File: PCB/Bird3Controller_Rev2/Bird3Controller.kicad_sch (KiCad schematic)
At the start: 49 parts, among them IC2 LM3519MK-20_NOPB, IC3 LM3405AXMY_NOPB, J1 Bird 3 24-pin Connector, J2 TXW154028S0 Connector, J3 2171800001, SW1 SW_Boot, SW2 SW_Reset, U1 ESP32-S3-WROOM-1, U3 SN65HVD231, U4 LMR36520ADDAR

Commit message: Add 22-pin connector, new headlight circuit, etc. for Rev 2
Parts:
- removed C23: 10u, Capacitor_SMD:C_0805_2012Metric_Pad1.18x1.45mm_HandSolder, symbol Device:C_Small
- removed C24: 0.01u, Capacitor_SMD:C_0805_2012Metric_Pad1.18x1.45mm_HandSolder, symbol Device:C_Small
- removed C25, C26: 1u, Capacitor_SMD:C_0805_2012Metric_Pad1.18x1.45mm_HandSolder, symbol Device:C_Small
- removed C4: 4n7, Capacitor_SMD:C_0805_2012Metric_Pad1.18x1.45mm_HandSolder, symbol Device:C_Small
- removed D2: D_Small, Diode_SMD:D_0805_2012Metric_Pad1.15x1.40mm_HandSolder, symbol Device:D_Small
- removed D4: D_Schottky_Small, Diode_SMD:D_0805_2012Metric_Pad1.15x1.40mm_HandSolder, symbol Device:D_Schottky_Small
- removed D7: PRTR5V0U2X, Package_TO_SOT_SMD:SOT-143, symbol Power_Protection:PRTR5V0U2X
- removed IC3: LM3405AXMY_NOPB, Bird3Controller:SOP65P490X109-9N, symbol Bird3Controller:LM3405AXMY_NOPB
- removed J3: 2171800001, Bird3Controller:MOLEX_2171800001, symbol Bird3Controller:2171800001
- removed L5: 27u, Bird3Controller:SRR1240270M, symbol Device:L_Small
- removed R14: 0.953Ω, Resistor_SMD:R_0805_2012Metric_Pad1.20x1.40mm_HandSolder, symbol Device:R_Small_US
- removed R4: 1M, Resistor_SMD:R_0805_2012Metric_Pad1.20x1.40mm_HandSolder, symbol Device:R_Small_US
- added C8: 10u, Capacitor_SMD:C_0805_2012Metric_Pad1.18x1.45mm_HandSolder, symbol Device:C_Small
- added J3: 87832-2220, Bird3Controller:878322220, symbol Bird3Controller:Bird 3 22-Pin Connector
- added J4: ~, Bird3Controller:Adafruit USB-C Breakout, symbol Bird3Controller:Adafruit_4090_USBC_BOB
- added L1: 100u, Bird3Controller:SRR1240270M, symbol Device:L_Small
- added R7: 0.200Ω, Resistor_SMD:R_0805_2012Metric_Pad1.20x1.40mm_HandSolder, symbol Device:R_Small_US
- added TP1: LCD_BL+, Bird3Controller:TestPointBridge_2Pads_D1.5mm, symbol Bird3Controller:TestPoint_Junction
- added TP2: 3V3, Bird3Controller:TestPointBridge_2Pads_D1.5mm, symbol Bird3Controller:TestPoint_Junction
- added TP3: VIN, Bird3Controller:TestPointBridge_2Pads_D1.5mm, symbol Bird3Controller:TestPoint_Junction
- added TP4: LED+, Bird3Controller:TestPointBridge_2Pads_D1.5mm, symbol Bird3Controller:TestPoint_Junction
- added TP5: LED-, Bird3Controller:TestPointBridge_2Pads_D1.5mm, symbol Bird3Controller:TestPoint_Junction
- added TP_Boot1: TestPoint_2Pole, Bird3Controller:TestPoint_2Pads_D1.0mm, symbol Connector:TestPoint_2Pole
- added U2: ~, Bird3Controller:Diodes_SO-8EP, symbol Bird3Controller:AL8862
- D3: Digikey Part Number (none) -> 478-7800-1-ND; JLCPCB Part (none) -> C143773; Manufacturer_Name (none) -> KYOCERA AVX; Manufacturer_Part_Number (none) -> SD0805S020S1R0; Mouser Part Number (none) -> 581-SD0805S020S1R0; now fitted; now in the parts list
- L3: value SRR1260-100M -> 10u
- R13: Digikey Part Number 541-CRCW0805150KFKEACCT-ND -> (none); JLCPCB Part C2077224 -> (none)
- R2, R3: value 5k1 -> 10k; Digikey Part Number 541-CRCW08055K10FKEACCT-ND -> (none); JLCPCB Part C844854 -> (none); Manufacturer_Part_Number CRCW08055K10FKEAC -> CRCW080510K0JNEA; Mouser Part Number 71-CRCW08055K10FKEAC -> 71-CRCW0805J-10K-E3
- renumbered IC2 to U5
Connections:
- net +3.3V is gone; now on net +3V3: J2.4 (VDD), J2.5 (VDD)
- net +36V: now also D3.1 (K), C8.1, J3.2 (36V), R7.1, U2.4 (VIN)
- net +3V3: now also J3.13 (LBK_In), J3.16 (THR_In), J3.8 (RBK_In), TP2.1; no longer C18.1, C20.1, L3.2, R11.2, R12.2
- net +5V: now also J4.7 (VBUS)
- net BR1: now also J3.11 (LBK_Out)
- net BR2: now also J3.7 (RBK_Out)
- net CAN_H: now also J3.5 (CAN_H)
- net CAN_L: now also J3.6 (CAN_L)
- net GND: now also R2.1, R3.1, C8.2, J3.1 (GND), J3.14 (LBK_GND), J3.18 (THR_GND), J3.3 (RBK_GND), J3.4 (PWR_ENA), J4.8 (GNB), TP_Boot1.1, U2.2 (GND), U2.7 (GND), U2.9 (PAD); no longer J1.21 (SPK-), R2.2, R3.2
- net LCD_BL+: now also TP1.1; no longer C22.1, D1.1 (K), U5.3 (VOUT)
- net LCD_BL_SIG: now also R2.2, U1.10 (GPIO17); no longer U1.25 (GPIO48)
- net LCD_DB0: now also U1.28 (GPIO35); no longer U1.10 (GPIO17)
- net LCD_DB1: now also U1.29 (GPIO36); no longer U1.11 (GPIO18)
- net LCD_DB2: now also U1.30 (GPIO37); no longer U1.23 (GPIO21)
- net LCD_DB3: now also U1.31 (GPIO38); no longer U1.28 (GPIO35)
- net LCD_DB4: now also U1.32 (GPIO39); no longer U1.29 (GPIO36)
- net LCD_DB5: now also U1.33 (GPIO40); no longer U1.30 (GPIO37)
- net LCD_DB6: now also U1.34 (GPIO41); no longer U1.31 (GPIO38)
- net LCD_DB7: now also U1.35 (GPIO42); no longer U1.24 (GPIO47)
- net LCD_RD: now also U1.25 (GPIO48); no longer U1.9 (GPIO16)
- net LCD_WR: now also U1.24 (GPIO47); no longer U1.8 (GPIO15)
- net LED+: now also J3.20 (LED+), TP4.2 (1)
- net LED-: now also J3.22 (LED-), TP5.2 (1)
- net LED_SIG: now also R3.2, U2.8 (CTRL)
- net THR1: now also J3.15 (THR_Out1)
- net THR2: now also J3.17 (THR_Out2)
- net USB_D+: now also J4.3 (D+)
- net USB_D-: now also J4.4 (D-)
- net at SW1.3, SW1.4, U1.27 (GPIO0/Strap): now also TP_Boot1.2
- net at C14.1, C15.1, C16.1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: now also TP3.1; no longer D5.1 (K), D6.1 (K)
- net at D3.2 (A): now also L1.1, U2.5 (SW), U2.6 (SW)
- net SPK+: no longer names the net of J1.23 (SPK+)
- new net: C18.1, C20.1, L3.2, R11.2, R12.2, TP2.2 (1)
- new net: C22.1, D1.1 (K), TP1.2 (1), U5.3 (VOUT)
- new net: R7.2, TP4.1, U2.1 (SET)
- new net: L1.2, TP5.1
- new net: D5.1 (K), D6.1 (K), TP3.2 (1)
- no-connect marks 0 -> 13
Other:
- note added: "22-Pin Connector"
- note removed: "Desired Output: 217mA VOut: 2.85V VIn: 3.3V Duty Cycle: 86% Calculated output with 0.953Ω resistor: 215mA"
- moved on the sheet: C14, C15, C16, C17, C18, C19, C20, C7, D5, D6, L3, R11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

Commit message: Add circuit to selectively ground the `PWR_ENA` pin
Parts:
- added F1: Polyfuse_Small, Bird3Controller:FUSC1607X85N, symbol Bird3Controller:0ZCM0001FF2G - Polyfuse_Small
- added Q1: 2N7002A, Package_TO_SOT_SMD:TSOT-23, symbol Bird3Controller:2N7002A - Q_NMOS_GSD
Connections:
- net GND: now also Q1.3 (D); no longer J1.4 (PWR_ENA), J3.4 (PWR_ENA)
- net PWR_ENA_SIG: now reaches U1.11 (GPIO18)
- net PWR_ENA_SIG: now also Q1.1 (G)
- new net: F1.1, Q1.2 (S)
- new net PWR_ENA: F1.2, J1.4 (PWR_ENA), J3.4 (PWR_ENA)
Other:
- note added: "Power Enable"
- moved on the sheet: C8, D3, L1, R3, R7, TP4, TP5, U2

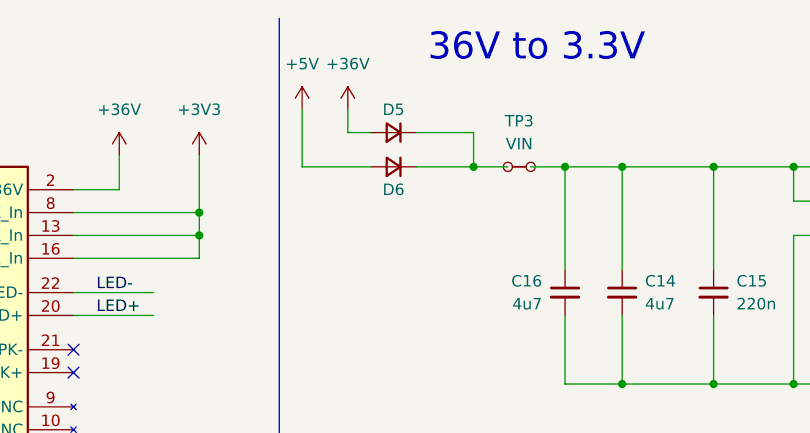
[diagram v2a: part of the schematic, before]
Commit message: Update PCB to use add PTC fuse on VIN
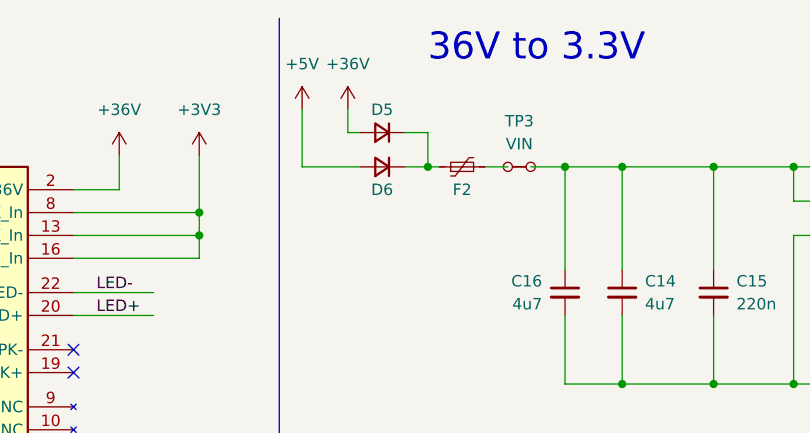
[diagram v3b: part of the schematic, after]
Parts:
- added F2: 0ZCF0100AF2A, FUSC7451X170N, symbol Bird3Controller:0ZCF0100AF2A
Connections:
- net at D5.1 (K), D6.1 (K): now also F2.1; no longer TP3.2 (1)
- new net: F2.2, TP3.2 (1)
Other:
- moved on the sheet: D5, D6

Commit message: Update PCB from schematic for first time since v8
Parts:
- F2: footprint FUSC7451X170N -> Bird3Controller:FUSC7451X170N
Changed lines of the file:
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@@
 			)
 		)
-		(property "Footprint" "FUSC7451X170N"
+		(property "Footprint" "Bird3Controller:FUSC7451X170N"
 			(at 252.73 125.4 0)
 			(effects
@@
 			)
 		)
-		(property "Description" ""
+		(property "Description" "Resettable Fuses - PPTC 1A 60V PPTC 2920 SMD"
 			(at 247.65 29.21 0)
 			(effects

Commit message: Add EEPROM to schematic and board.
Also add the symbol, footprint, and 3D model
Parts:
- added IC1: M24C08-RMN6TP, Bird3Controller:SOIC127P600X175-8N, symbol Bird3Controller:M24C08-RMN6TP
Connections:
- net +3V3: now also IC1.8 (VCC)
- net GND: now also IC1.3 (E2), IC1.4 (VSS), IC1.7 (~{WC})
- net SCL: now reaches U1.36 (GPIO44/RX)
- net SCL: now also IC1.6 (SCL)
- net SDA: now reaches U1.37 (GPIO43/TX)
- net SDA: now also IC1.5 (SDA)
- no-connect marks 13 -> 15
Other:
- note added: "EEPROM"

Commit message: Add Mouser links and prices for all components
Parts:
- C1, C3: value 0.1u -> 100n; Mouser Price QTY1 (none) -> 0.10; Mouser Price QTY10 (none) -> 0.065; Mouser Price/Stock (none) -> https://www.mouser.com/ProductDetail/YAGEO/AC0805JRX7R9BB10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
- C14, C16, C21: Mouser Price QTY1 (none) -> 0.68; Mouser Price QTY10 (none) -> 0.475; Mouser Price/Stock (none) -> https://www.mouser.com/ProductDetail/Samsung-Electro-Mechan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
- C15: Mouser Price QTY1 (none) -> 0.11; Mouser Price QTY10 (none) -> 0.078; Mouser Price/Stock (none) -> https://www.mouser.com/ProductDetail/KYOCERA-AVX/08053C224K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
- C17, C22: Mouser Price QTY1 (none) -> 0.10; Mouser Price QTY10 (none) -> 0.027; Mouser Price/Stock (none) -> https://www.mouser.com/ProductDetail/Samsung-Electro-Mechan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
- C18, C20: Mouser Price QTY1 (none) -> 0.87; Mouser Price QTY10 (none) -> 0.55; Mouser Price/Stock (none) -> https://www.mouser.com/ProductDetail/Samsung-Electro-Mechan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
- C19: Mouser Price QTY1 (none) -> 0.10; Mouser Price QTY10 (none) -> 0.065; Mouser Price/Stock (none) -> https://www.mouser.com/ProductDetail/YAGEO/AC0805JRX7R9BB10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
- C2: Mouser Price QTY1 (none) -> 0.39; Mouser Price QTY10 (none) -> 0.196; Mouser Price/Stock (none) -> https://www.mouser.com/ProductDetail/Murata-Electronics/GRT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
- C7: Mouser Price QTY1 (none) -> 0.10; Mouser Price QTY10 (none) -> 0.058; Mouser Price/Stock (none) -> https://www.mouser.com/ProductDetail/KYOCERA-AVX/08055C472K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
- C8: Mouser Price QTY1 (none) -> 0.35; Mouser Price QTY10 (none) -> 0.199; Mouser Price/Stock (none) -> https://www.mouser.com/ProductDetail/Murata-Electronics/GRT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
- D1, D3: Mouser Price QTY1 (none) -> 0.32; Mouser Price QTY10 (none) -> 0.252; Mouser Price/Stock (none) -> https://www.mouser.com/ProductDetail/KYOCERA-AVX/SD0805S020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
- D5, D6: Mouser Price QTY1 (none) -> 0.21; Mouser Price QTY10 (none) -> 0.148; Mouser Price/Stock https://www.mouser.co.uk/ProductDetail/Panjit/GS1J_R1_00001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 -> https://www.mouser.com/ProductDetail/Panjit/GS1J_R1_00001?q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
- F1: Manufacture Part Number 0ZCM0001FF2G -> (none); Manufacturer Bel Fuse -> (none); Manufacturer_Name (none) -> Bel Fuse; Manufacturer_Part_Number (none) -> 0ZCM0001FF2G; Mouser Price QTY1 (none) -> 0.19; Mouser Price QTY10 (none) -> 0.16; Mouser Price/Stock (none) -> https://www.mouser.com/ProductDetail/Bel-Fuse/0ZCM0001FF2G?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
- F2: Manufacturer Part Number 0ZCF0100AF2A -> (none); Mouser Price QTY1 (none) -> 0.55; Mouser Price QTY10 (none) -> 0.454
- IC1: Manufacturer STMicroelectronics -> (none); Manufacturer Part Number M24C08-RMN6TP -> (none); Manufacturer_Name (none) -> STMicroelectronics; Manufacturer_Part_Number (none) -> M24C08-RMN6TP; Mouser Price QTY1 (none) -> 0.19; Mouser Price QTY10 (none) -> 0.175
- J1: Mouser Price QTY1 (none) -> 2.05; Mouser Price QTY10 (none) -> 1.79; Mouser Price/Stock (none) -> https://www.mouser.com/ProductDetail/Molex/87832-6123?qs=Vr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
- J2: Mouser Price QTY1 (none) -> 1.24; Mouser Price QTY10 (none) -> 1.05; Mouser Price/Stock https://www.mouser.co.uk/ProductDetail/Hirose-Connector/FH3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 -> https://www.mouser.com/ProductDetail/Hirose-Connector/FH34S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
- J3: Manufacturer_Part_Number 87832-2220 -> 87832-6062; Mouser Part Number 538-87832-2220 -> 538-87832-6062; Mouser Price QTY1 (none) -> 3.27; Mouser Price QTY10 (none) -> 2.98; Mouser Price/Stock https://www.mouser.com/Search/Refine.aspx?Keyword=538-87832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 -> https://www.mouser.com/ProductDetail/Molex/87832-6062?qs=yd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
- J4: Manufacturer Adafruit -> (none); Manufacturer Part Number 4090 -> (none); Manufacturer_Name (none) -> Adafruit; Manufacturer_Part_Number (none) -> 4090; Mouser Part Number (none) -> 485-4090; Mouser Price QTY1 (none) -> 2.95; Mouser Price QTY10 (none) -> 2.95; Mouser Price/Stock (none) -> https://www.mouser.com/ProductDetail/Adafruit/4090?qs=2WXla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
- L1: Mouser Price QTY1 (none) -> 0.64; Mouser Price QTY10 (none) -> 0.634; Mouser Price/Stock (none) -> https://www.mouser.com/ProductDetail/Bourns/SRR1240-101M?qs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
- L3: Mouser Price QTY1 (none) -> 1.27; Mouser Price QTY10 (none) -> 0.909; Mouser Price/Stock https://www.mouser.co.uk/ProductDetail/Bourns/SRR1260-100M?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 -> https://www.mouser.com/ProductDetail/Bourns/SRR1260-100M?qs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
- L4: Mouser Price QTY1 (none) -> 0.11; Mouser Price QTY10 (none) -> 0.107; Mouser Price/Stock (none) -> https://www.mouser.com/ProductDetail/Bourns/CVH252009-2R2M?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
- Q1: Manufacturer Diotec -> (none); Manufacturer Part Number 2N7002A -> (none); Manufacturer_Name (none) -> Diotec; Manufacturer_Part_Number (none) -> 2N7002A; Mouser Price QTY1 (none) -> 0.11; Mouser Price QTY10 (none) -> 0.081; Mouser Price/Stock (none) -> https://www.mouser.com/ProductDetail/Diotec-Semiconductor/2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
- R1: Mouser Price QTY1 (none) -> 0.10; Mouser Price QTY10 (none) -> 0.02; Mouser Price/Stock (none) -> https://www.mouser.com/ProductDetail/Vishay-Dale/CRCW08054K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
- R11, R12: Mouser Price QTY1 (none) -> 0.13; Mouser Price QTY10 (none) -> 0.063; Mouser Price/Stock (none) -> https://www.mouser.com/ProductDetail/Vishay-Dale/RCS0805100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
- R13: Mouser Price QTY1 (none) -> 0.11; Mouser Price QTY10 (none) -> 0.052; Mouser Price/Stock (none) -> https://www.mouser.com/ProductDetail/Vishay-Dale/CRCW080543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
- R2, R3: Mouser Price QTY1 (none) -> 0.10; Mouser Price QTY10 (none) -> 0.019; Mouser Price/Stock (none) -> https://www.mouser.com/ProductDetail/Vishay-Dale/CRCW080510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
- R5, R6: Mouser Price QTY1 (none) -> 0.13; Mouser Price QTY10 (none) -> 0.043; Mouser Price/Stock (none) -> https://www.mouser.com/ProductDetail/Vishay-Dale/RCS080560R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
- R7: Mouser Price QTY1 (none) -> 0.26; Mouser Price QTY10 (none) -> 0.221; Mouser Price/Stock (none) -> https://www.mouser.com/ProductDetail/TE-Connectivity-CGS/RL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
- S1: Mouser Price QTY1 (none) -> 0.16; Mouser Price QTY10 (none) -> 0.148; Mouser Price/Stock https://www.mouser.co.uk/ProductDetail/CK/PTS636-SK43-SMTR-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 -> https://www.mouser.com/ProductDetail/CK/PTS636-SK43-SMTR-LF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
- SW1, SW2: Mouser Price QTY1 (none) -> 0.14; Mouser Price QTY10 (none) -> 0.13; Mouser Price/Stock https://www.mouser.co.uk/ProductDetail/CK/PTS526-SK15-SMTR2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 -> https://www.mouser.com/ProductDetail/CK/PTS526-SK15-SMTR2-L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
- TP1, TP2, TP3, TP4, TP5, TP_Boot1: now left out of the parts list
- U1: Mouser Price QTY1 (none) -> 3.62; Mouser Price QTY10 (none) -> 3.62; Mouser Price/Stock (none) -> https://www.mouser.com/ProductDetail/Espressif-Systems/ESP3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
- U2: Manufacture Part Number AL8862SP-13 -> (none); Manufacturer Diodes -> (none); Manufacturer_Name (none) -> Diodes; Manufacturer_Part_Number (none) -> AL8862SP-13; Mouser Price QTY1 (none) -> 0.93; Mouser Price QTY10 (none) -> 0.748; Mouser Price/Stock (none) -> https://www.mouser.com/ProductDetail/Diodes-Incorporated/AL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
- U3: Mouser Price QTY1 (none) -> 2.51; Mouser Price QTY10 (none) -> 2.25; Mouser Price/Stock (none) -> https://www.mouser.com/ProductDetail/Texas-Instruments/SN65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
- U4: Mouser Price QTY1 (none) -> 2.72; Mouser Price QTY10 (none) -> 2.39; Mouser Price/Stock (none) -> https://www.mouser.com/ProductDetail/Texas-Instruments/LMR3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
- U5: Mouser Price QTY1 (none) -> 2.02; Mouser Price QTY10 (none) -> 1.72; Mouser Price/Stock https://www.mouser.co.uk/ProductDetail/Texas-Instruments/LM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 -> https://www.mouser.com/ProductDetail/Texas-Instruments/LM35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
